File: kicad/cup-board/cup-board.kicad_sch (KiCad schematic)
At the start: 102 parts, among them J10 MK2 flex (IM73A135), J11 MK3 flex (IM72D128 PDM), J12 BOOM_ELECTRET (solder pads, p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, J2 EARCUP_SPKR, J7 CUP_IN (A2B + panel audio + b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, J8 CUP_OUT (A2B to next cup), J9 MK1 flex (IM73A135 FF/FB), Q1 AO3401A, Q2 MMBT3904, U1 ADAU1861, U2 LSM6DSV16BX, U3 MAXM86161, U4 AQW612S, U5 AQW612S, U6 AD2428WBCPZ (sub-node), U7 TPS62161DSG (1V8), U8 ADP7118AUJZ-3.3-R7 (3V3_MIC), U9 ADP7118AUJZ-3.3-R7 (VLED)

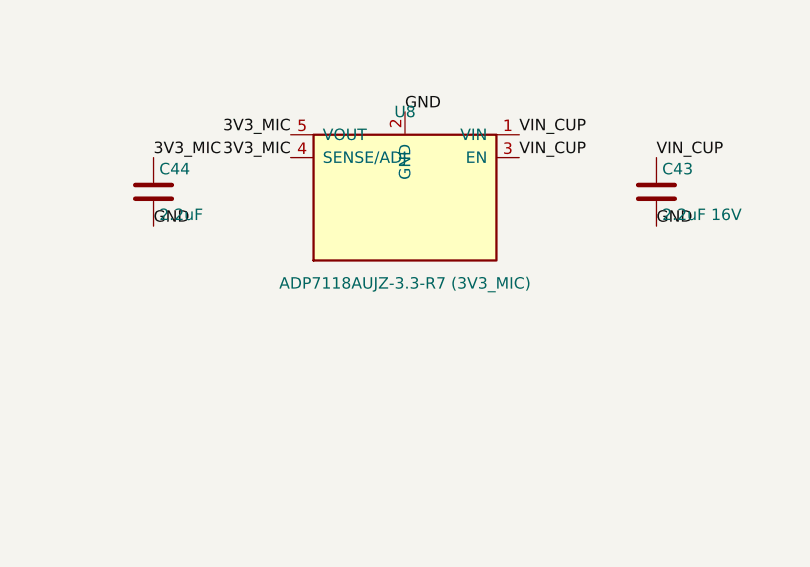
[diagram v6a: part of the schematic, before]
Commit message: [LIMA] cup board: U8 -> ADP7118AUJZ-2.5, value only - mic rail now 2.5 V, inside the IM73A135's limits
U8 was the 3.3 V ADP7118, putting 3.3 V on MK1/MK2 against the IM73A135's
3.0 V absolute maximum (DS v1.20 Table 5). Now the 2.5 V version: same
symbol, same TSOT-23-5 footprint, 2.5 V inside the 2.3-3.0 V normal-mode
range. Per Peter, the net keeps the name 3V3_MIC so the routed PCB's nets,
net class and tracks don't change (the earlier rename was rolled back).

design_nets.py check OK; ERC 0 errors; PCB DRC with parity 0 errors,
0 unconnected. One expected parity warning: the PCB's U8 still shows the
old value text until it is set in pcbnew.

Co-Authored-By: Claude Opus 5.5 <noreply@anthropic.com>
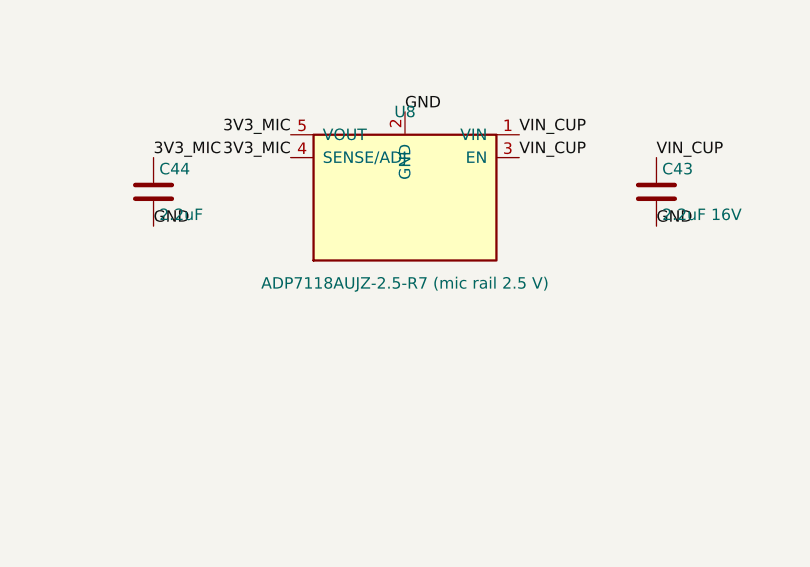
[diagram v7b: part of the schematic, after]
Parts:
- U8: value ADP7118AUJZ-3.3-R7 (3V3_MIC) -> ADP7118AUJZ-2.5-R7 (mic rail 2.5 V)
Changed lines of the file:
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@@
 			)
 		)
-		(property "Value" "ADP7118AUJZ-3.3-R7 (3V3_MIC)"
+		(property "Value" "ADP7118AUJZ-2.5-R7 (mic rail 2.5 V)"
 			(at 233.68 330.2 0)
 			(effects
